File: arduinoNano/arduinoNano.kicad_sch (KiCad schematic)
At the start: 20 parts, among them J1 USB_B_Mini, SW1 SW_Push, U1 LM1117MP-5.0, U2 ATmega328P-M, Y1 16MHz

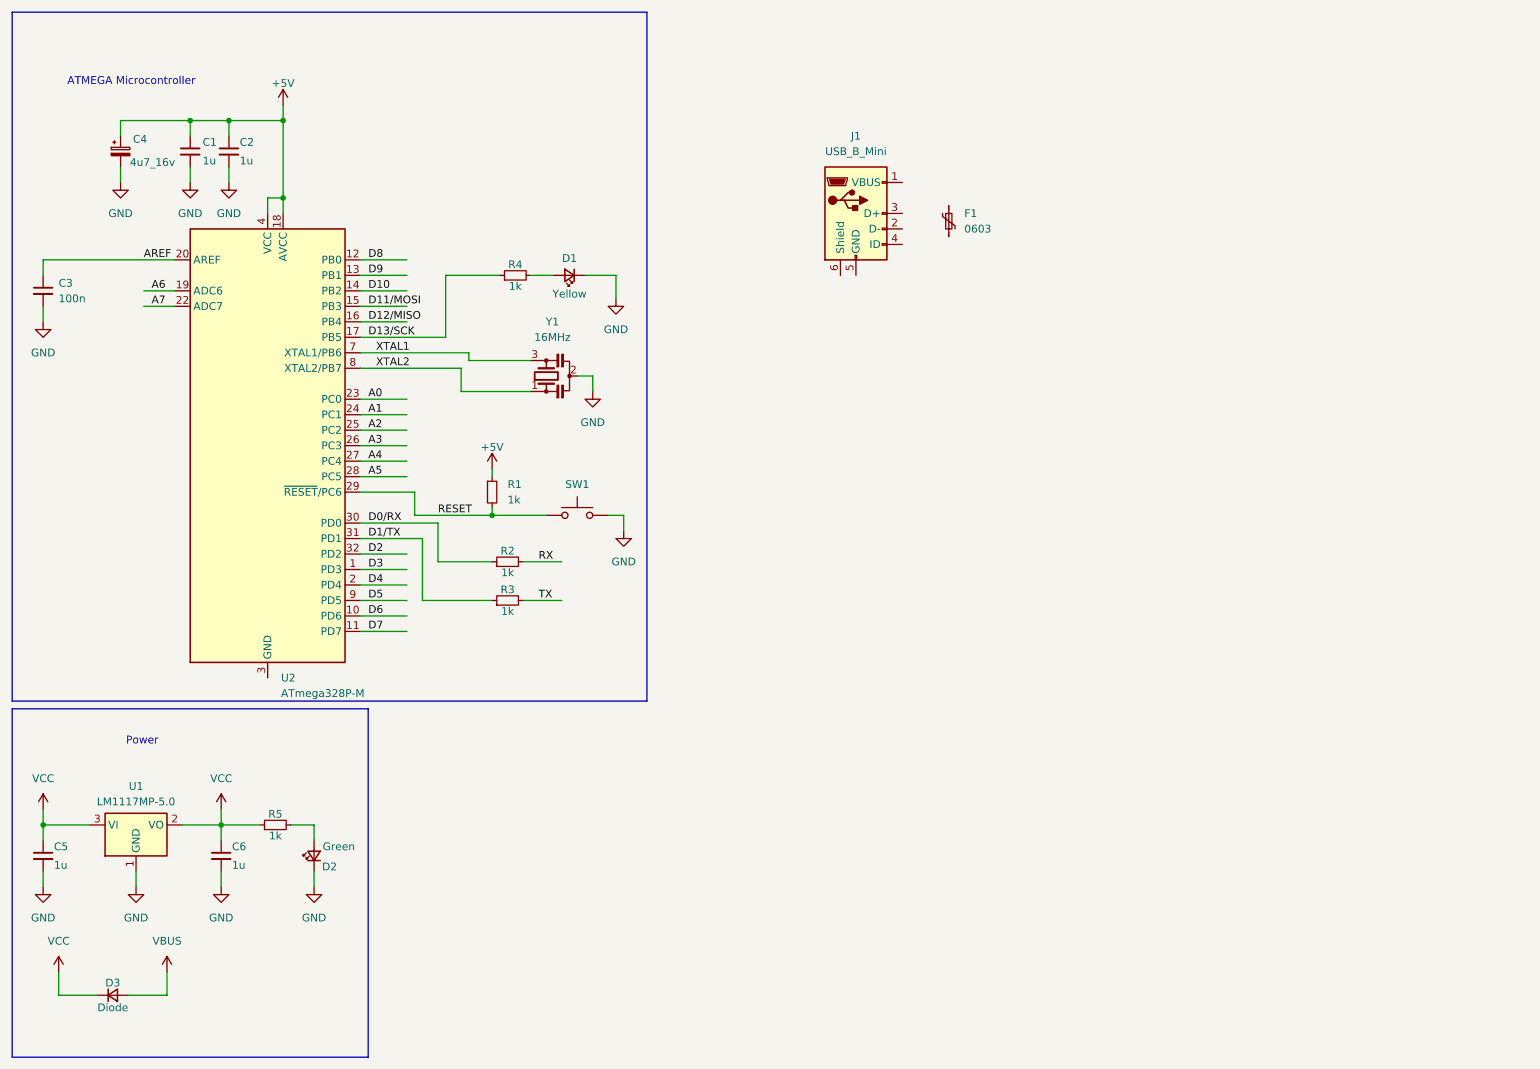
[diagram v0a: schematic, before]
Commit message: done schematic. still in pcb designing not done yet
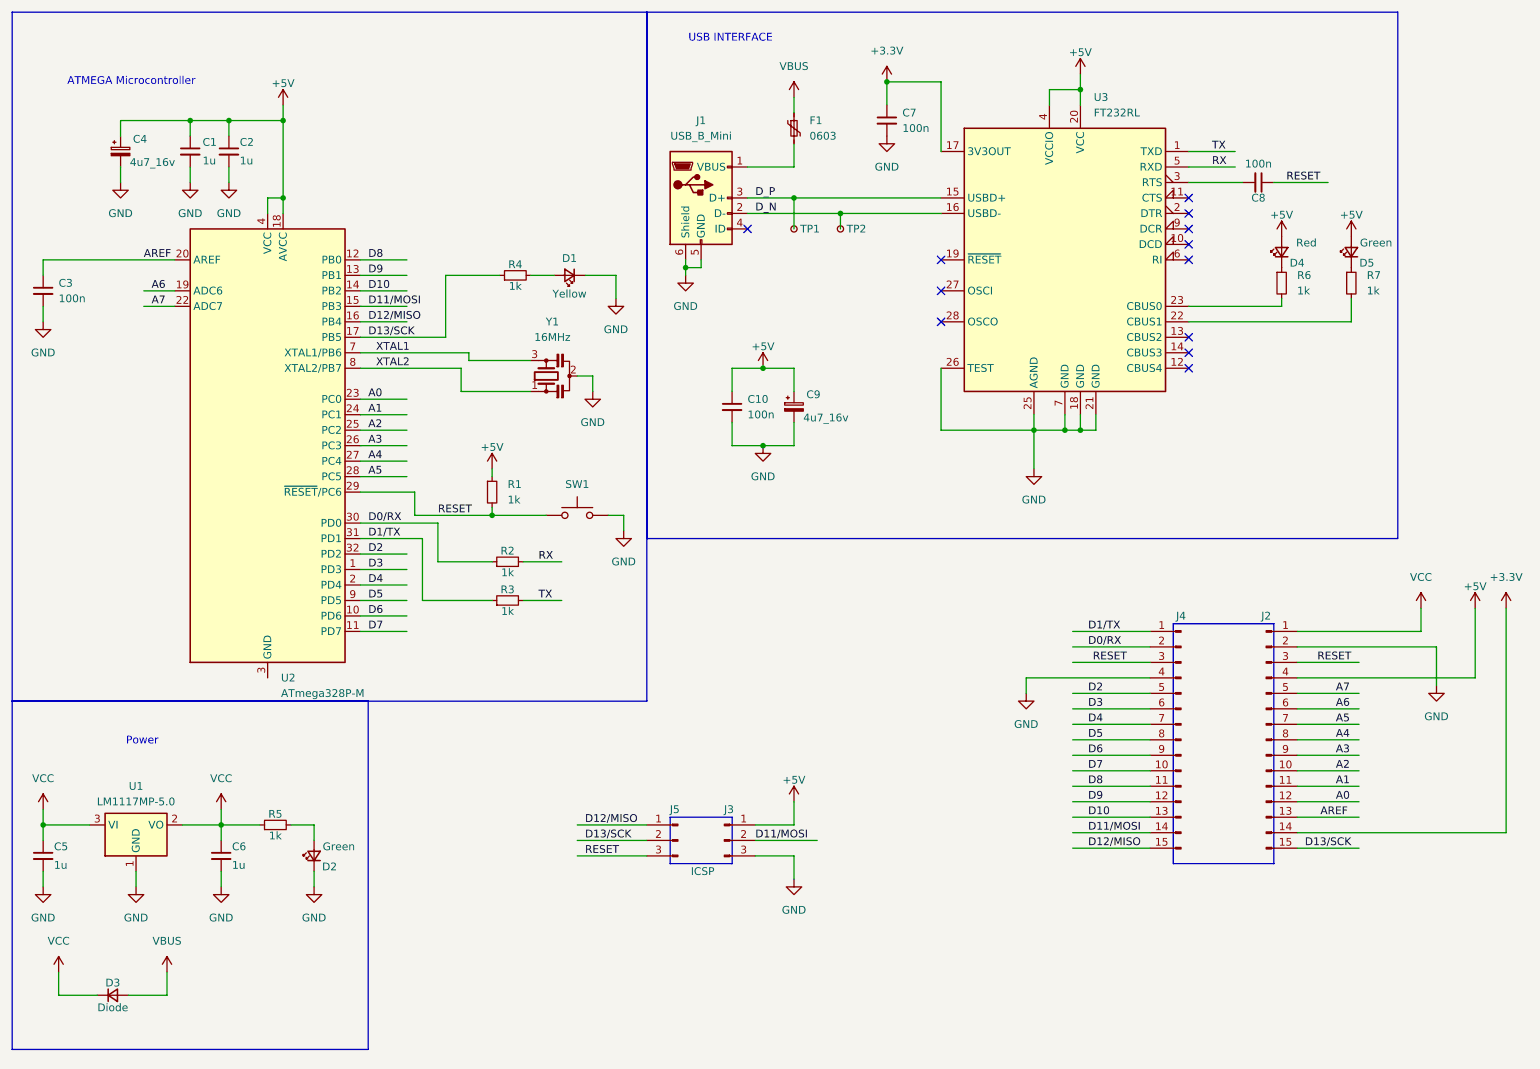
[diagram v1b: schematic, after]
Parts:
- added C10, C7, C8: 100n, Capacitor_SMD:C_0603_1608Metric, symbol Device:C_Small
- added C9: 4u7_16v, Capacitor_Tantalum_SMD:CP_EIA-3216-10_Kemet-I, symbol Device:C_Polarized_Small
- added D4: Red, LED_SMD:LED_0805_2012Metric, symbol Device:LED_Small
- added D5: Green, LED_SMD:LED_0805_2012Metric, symbol Device:LED_Small
- added J2, J4: Conn_01x15_Pin, Connector_PinHeader_2.54mm:PinHeader_1x15_P2.54mm_Vertical, symbol Connector:Conn_01x15_Pin
- added J3, J5: ICSP, Connector_PinHeader_2.54mm:PinHeader_1x03_P2.54mm_Vertical, symbol Connector:Conn_01x03_Pin
- added R6, R7: 1k, Diode_SMD:D_0603_1608Metric, symbol Device:R_Small
- added TP1, TP2: TestPoint_Small, TestPoint:TestPoint_Pad_D1.0mm, symbol Connector:TestPoint_Small
- added U3: FT232RL, Package_SO:SSOP-28_5.3x10.2mm_P0.65mm, symbol Interface_USB:FT232RL
- C1, C2, C3, C5, C6: footprint (none) -> Capacitor_SMD:C_0603_1608Metric
- C4: footprint (none) -> Capacitor_Tantalum_SMD:CP_EIA-3216-10_Kemet-I
- D1, D2: footprint (none) -> LED_SMD:LED_0805_2012Metric
- D3: footprint (none) -> Diode_SMD:D_MicroSMP_AK
- F1, R1, R2, R3, R4, R5: footprint (none) -> Diode_SMD:D_0603_1608Metric
- J1: footprint (none) -> Connector_USB:USB_Mini-B_Lumberg_2486_01_Horizontal
- SW1: footprint (none) -> Button_Switch_SMD:Panasonic_EVQPUJ_EVQPUA
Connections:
- net +5V: now also C10.1, C9.1, D4.2 (A), D5.2 (A), J2.4 (Pin_4), J3.1 (Pin_1), U3.20 (VCC), U3.4 (VCCIO)
- net A0: now also J2.12 (Pin_12)
- net A1: now also J2.11 (Pin_11)
- net A2: now also J2.10 (Pin_10)
- net A3: now also J2.9 (Pin_9)
- net A4: now also J2.8 (Pin_8)
- net A5: now also J2.7 (Pin_7)
- net A6: now also J2.6 (Pin_6)
- net A7: now also J2.5 (Pin_5)
- net AREF: now also J2.13 (Pin_13)
- net D0/RX: now also J4.2 (Pin_2)
- net D10: now also J4.13 (Pin_13)
- net D11/MOSI: now also J3.2 (Pin_2), J4.14 (Pin_14)
- net D12/MISO: now also J4.15 (Pin_15), J5.1 (Pin_1)
- net D13/SCK: now also J2.15 (Pin_15), J5.2 (Pin_2)
- net D1/TX: now also J4.1 (Pin_1)
- net D2: now also J4.5 (Pin_5)
- net D3: now also J4.6 (Pin_6)
- net D4: now also J4.7 (Pin_7)
- net D5: now also J4.8 (Pin_8)
- net D6: now also J4.9 (Pin_9)
- net D7: now also J4.10 (Pin_10)
- net D8: now also J4.11 (Pin_11)
- net D9: now also J4.12 (Pin_12)
- net GND: now also J1.5 (GND), J1.6 (Shield), C10.2, C7.2, C9.2, J2.2 (Pin_2), J3.3 (Pin_3), J4.4 (Pin_4), U3.18 (GND), U3.21 (GND), U3.25 (AGND), U3.26 (TEST), U3.7 (GND)
- net RESET: now also C8.1, J2.3 (Pin_3), J4.3 (Pin_3), J5.3 (Pin_3)
- net RX: now also U3.5 (RXD)
- net TX: now also U3.1 (TXD)
- net VBUS: now also F1.1
- net VCC: now also J2.1 (Pin_1)
- net at J1.1 (VBUS): now also F1.2
- net D_N: now reaches J1.2 (D-)
- net D_N: now also TP2.1, U3.16 (USBD-)
- net D_P: now reaches J1.3 (D+)
- net D_P: now also TP1.1, U3.15 (USBD+)
- new net: C8.2, U3.3 (RTS)
- new net: D4.1 (K), R6.1
- new net: R6.2, U3.23 (CBUS0)
- new net: R7.2, U3.22 (CBUS1)
- new net: D5.1 (K), R7.1
- new net +3.3V: C7.1, J2.14 (Pin_14), U3.17 (3V3OUT)
- no-connect marks 0 -> 12
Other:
- note added: "USB INTERFACE"
- moved on the sheet: F1, J1
